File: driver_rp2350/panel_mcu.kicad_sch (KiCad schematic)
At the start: 33 parts, among them SW1 SW_Push, SW2 SW_Push, U1 APS6404L-3SQR, U2 RP2354B_80QFN, Y1 ABM8-272-T3

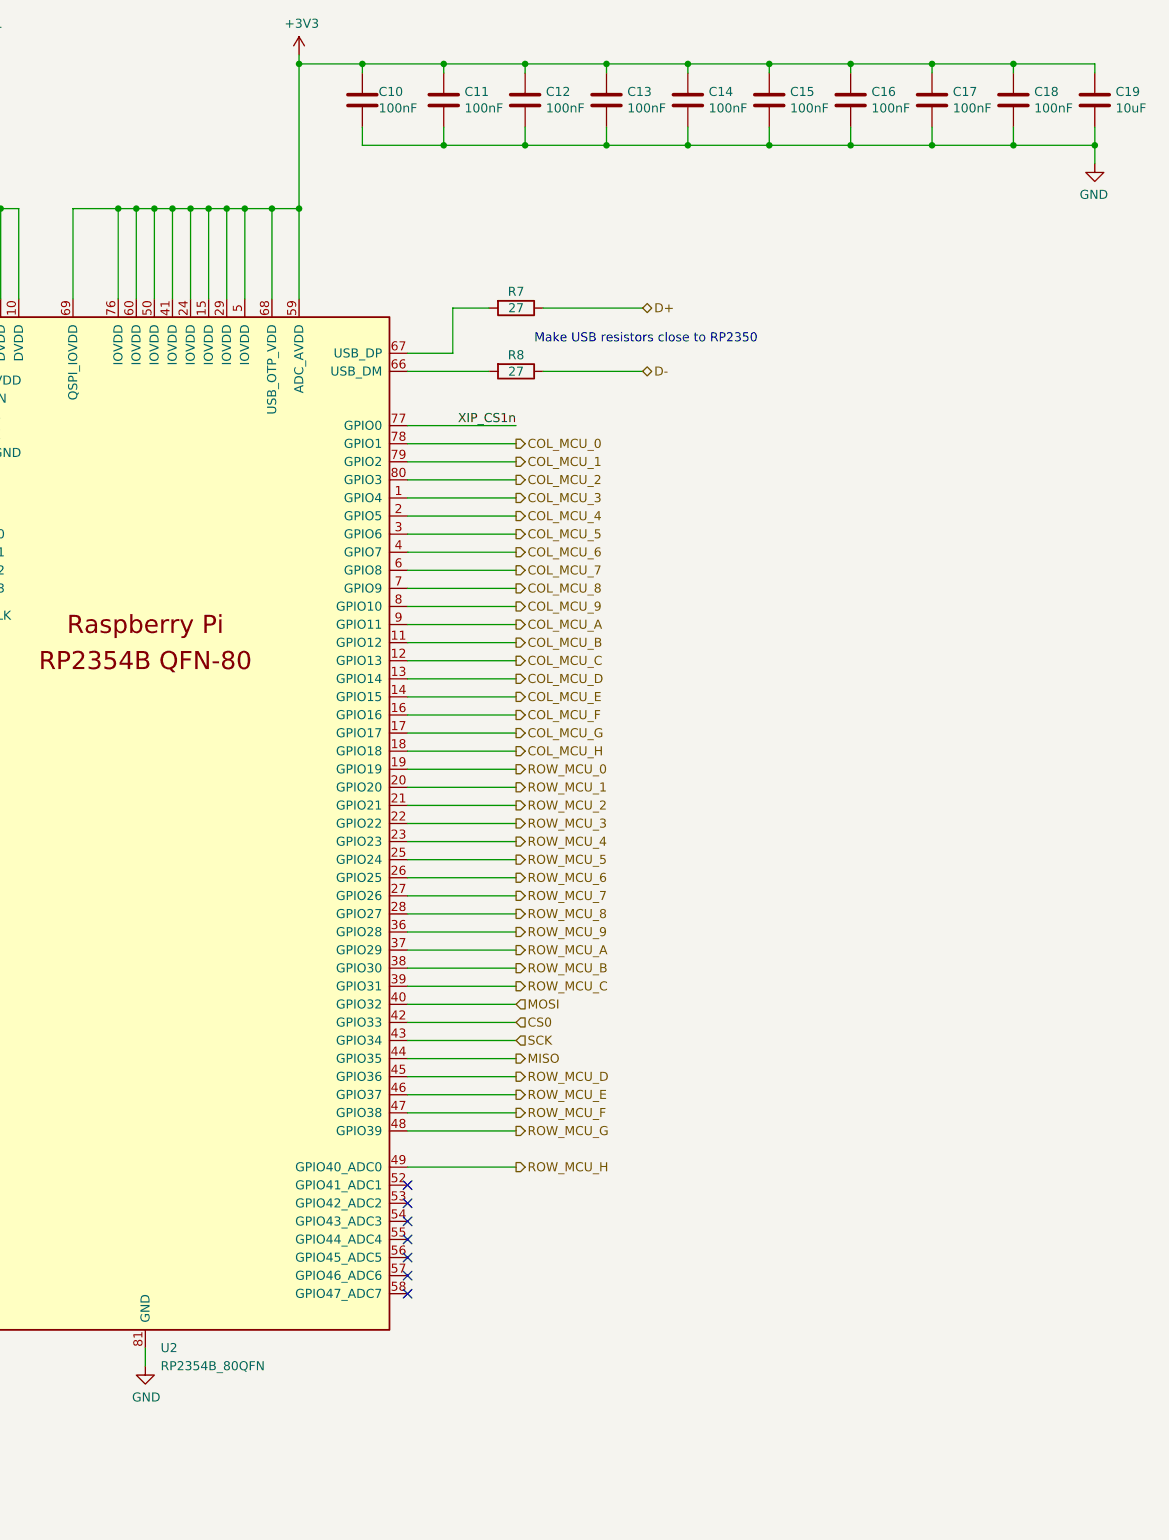
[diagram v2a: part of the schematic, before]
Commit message: Worked on layout for 18x18 rp2354b panels.
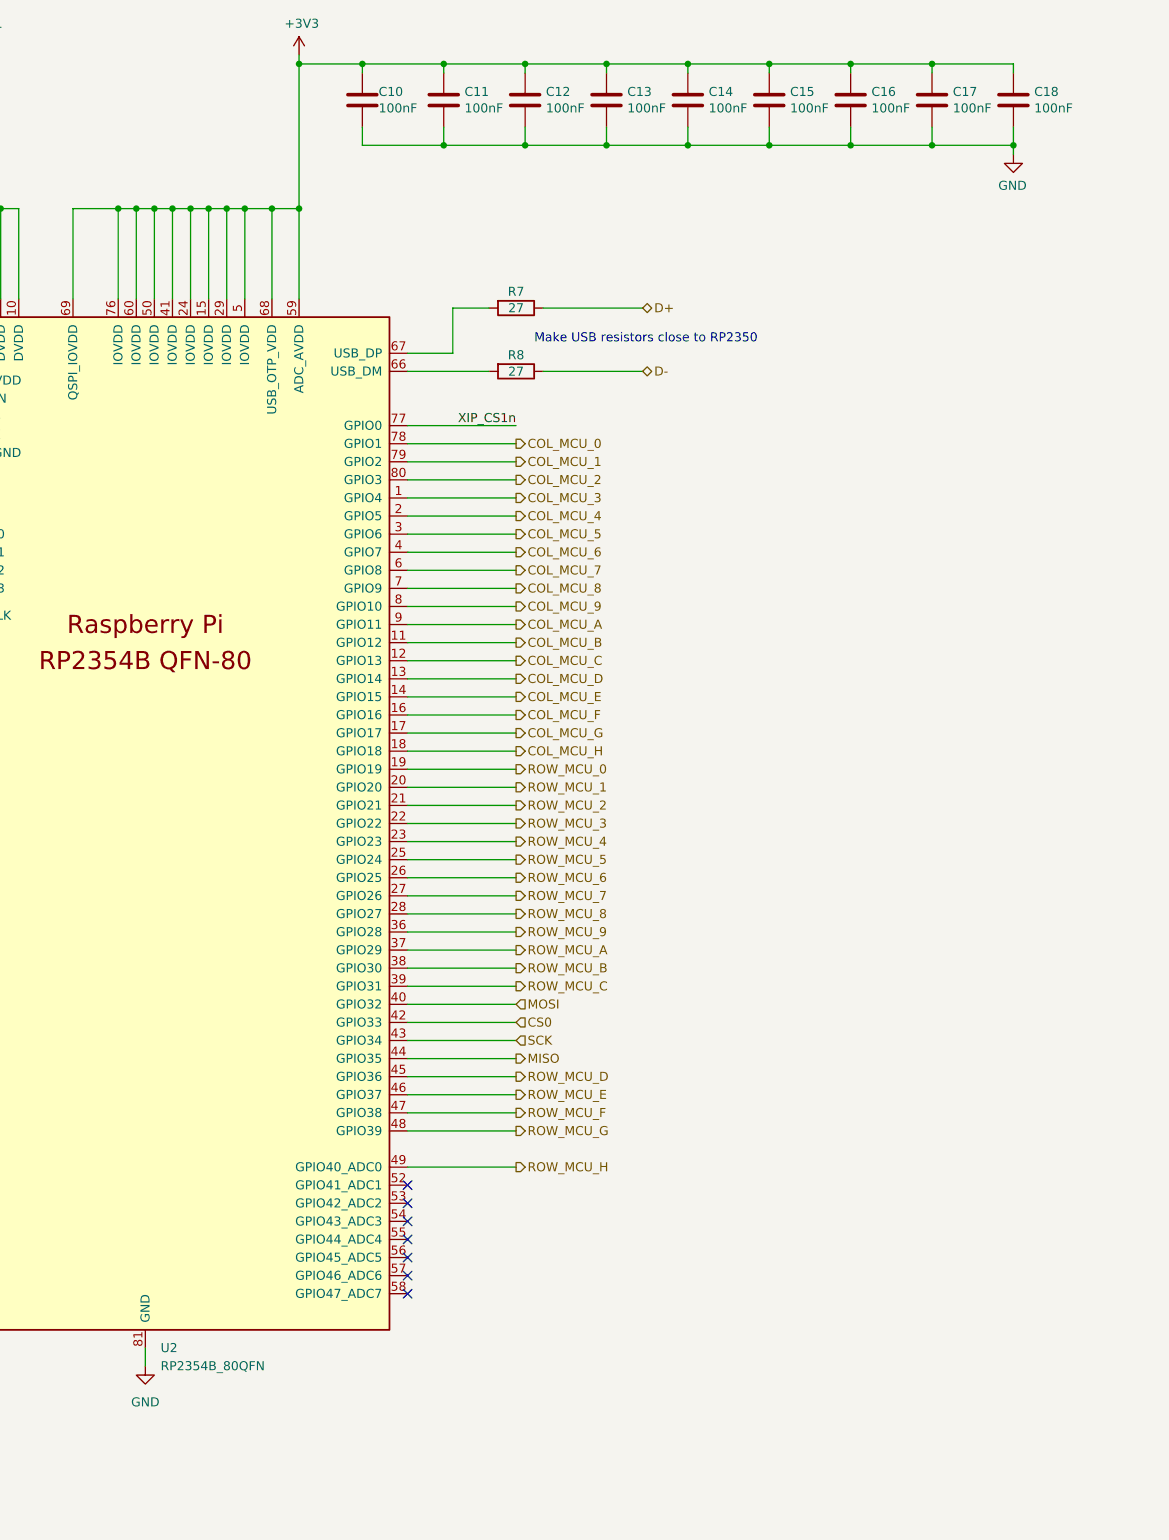
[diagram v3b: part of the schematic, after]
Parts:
- removed C19: 10uF, Capacitor_SMD:C_0402_1005Metric, symbol Device:C
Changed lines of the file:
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@@
 	)
 	(junction
-		(at 326.39 31.75)
-		(diameter 0)
-		(color 0 0 0 0)
-	)
-	(junction
 		(at 222.25 52.07)
 		(diameter 0)
@@
 	)
 	(junction
+		(at 326.39 43.18)
+		(diameter 0)
+		(color 0 0 0 0)
+	)
+	(junction
 		(at 140.97 73.66)
 		(diameter 0)
@@
 	)
 	(junction
-		(at 337.82 43.18)
-		(diameter 0)
-		(color 0 0 0 0)
-	)
-	(junction
 		(at 292.1 43.18)
 		(diameter 0)
@@
 	)
 	(junction
-		(at 326.39 43.18)
-		(diameter 0)
-		(color 0 0 0 0)
-	)
-	(junction
 		(at 280.67 31.75)
 		(diameter 0)
@@
 	(wire
 		(pts
+			(xy 326.39 43.18) (xy 326.39 44.45)
+		)
+		(stroke
+			(width 0)
+			(type default)
+		)
+	)
+	(wire
+		(pts
 			(xy 241.3 92.71) (xy 256.54 92.71)
 		)
@@
 	(wire
 		(pts
-			(xy 326.39 31.75) (xy 337.82 31.75)
-		)
-		(stroke
-			(width 0)
-			(type default)
-		)
-	)
-	(wire
-		(pts
 			(xy 241.3 135.89) (xy 256.54 135.89)
 		)
@@
 	(wire
 		(pts
-			(xy 337.82 43.18) (xy 337.82 45.72)
-		)
-		(stroke
-			(width 0)
-			(type default)
-		)
-	)
-	(wire
-		(pts
 			(xy 181.61 52.07) (xy 181.61 64.77)
 		)
@@
 	(wire
 		(pts
-			(xy 337.82 40.64) (xy 337.82 43.18)
-		)
-		(stroke
-			(width 0)
-			(type default)
-		)
-	)
-	(wire
-		(pts
 			(xy 158.75 100.33) (xy 172.72 100.33)
 		)
@@
 	(wire
 		(pts
-			(xy 337.82 31.75) (xy 337.82 33.02)
-		)
-		(stroke
-			(width 0)
-			(type default)
-		)
-	)
-	(wire
-		(pts
 			(xy 204.47 212.09) (xy 204.47 214.63)
 		)
@@
 	(wire
 		(pts
-			(xy 337.82 43.18) (xy 326.39 43.18)
-		)
-		(stroke
-			(width 0)
-			(type default)
-		)
-	)
-	(wire
-		(pts
 			(xy 68.58 170.18) (xy 82.55 170.18)
 		)
@@
 	)
 	(symbol
-		(lib_id "power:GND")
-		(at 204.47 214.63 0)
-		(unit 1)
-		(exclude_from_sim no)
-		(in_bom yes)
-		(on_board yes)
-		(dnp no)
-		(property "Reference" "#PWR018"
-			(at 204.47 220.98 0)
-			(effects
-				(font
-					(size 1.27 1.27)
-				)
-				(hide yes)
-			)
-		)
-		(property "Value" "GND"
-			(at 204.597 219.0242 0)
-			(effects
-				(font
-					(size 1.27 1.27)
-				)
-			)
-		)
-		(property "Footprint" ""
-			(at 204.47 214.63 0)
-			(effects
-				(font
-					(size 1.27 1.27)
-				)
-				(hide yes)
-			)
-		)
-		(property "Datasheet" ""
-			(at 204.47 214.63 0)
-			(effects
-				(font
-					(size 1.27 1.27)
-				)
-				(hide yes)
-			)
-		)
-		(property "Description" ""
-			(at 204.47 214.63 0)
-			(effects
-				(font
-					(size 1.27 1.27)
-				)
-			)
-		)
-		(pin "1"
-		)
-		(instances
-			(project "driver_rp2350"
-				(path "/1e634561-32a0-4ffa-9d4f-e93f355464d5/b30b56c6-21ca-46ed-bb1a-e5062fd43ea8"
-					(reference "#PWR018")
-					(unit 1)
-				)
-			)
-		)
-	)
-	(symbol
 		(lib_id "power:+3V3")
 		(at 226.06 30.48 0)
@@
 	)
 	(symbol
-		(lib_id "Device:C")
-		(at 337.82 36.83 0)
-		(unit 1)
-		(exclude_from_sim no)
-		(in_bom yes)
-		(on_board yes)
-		(dnp no)
-		(property "Reference" "C19"
-			(at 340.741 35.6616 0)
-			(effects
-				(font
-					(size 1.27 1.27)
-				)
-				(justify left)
-			)
-		)
-		(property "Value" "10uF"
-			(at 340.741 37.973 0)
-			(effects
-				(font
-					(size 1.27 1.27)
-				)
-				(justify left)
-			)
-		)
-		(property "Footprint" "Capacitor_SMD:C_0402_1005Metric"
-			(at 338.7852 40.64 0)
-			(effects
-				(font
-					(size 1.27 1.27)
-				)
-				(hide yes)
-			)
-		)
-		(property "Datasheet" "~"
-			(at 337.82 36.83 0)
-			(effects
-				(font
-					(size 1.27 1.27)
-				)
-				(hide yes)
-			)
-		)
-		(property "Description" ""
-			(at 337.82 36.83 0)
-			(effects
-				(font
-					(size 1.27 1.27)
-				)
-			)
-		)
-		(pin "1"
-		)
-		(pin "2"
-		)
-		(instances
-			(project "driver_rp2350"
-				(path "/1e634561-32a0-4ffa-9d4f-e93f355464d5/b30b56c6-21ca-46ed-bb1a-e5062fd43ea8"
-					(reference "C19")
-					(unit 1)
-				)
-			)
-		)
-	)
-	(symbol
 		(lib_id "power:+3V3")
 		(at 68.58 151.13 0)
@@
 	)
 	(symbol
+		(lib_name "GND_1")
+		(lib_id "power:GND")
+		(at 204.47 214.63 0)
+		(unit 1)
+		(exclude_from_sim no)
+		(in_bom yes)
+		(on_board yes)
+		(dnp no)
+		(fields_autoplaced yes)
+		(property "Reference" "#PWR03"
+			(at 204.47 220.98 0)
+			(effects
+				(font
+					(size 1.27 1.27)
+				)
+				(hide yes)
+			)
+		)
+		(property "Value" "GND"
+			(at 204.47 219.71 0)
+			(effects
+				(font
+					(size 1.27 1.27)
+				)
+			)
+		)
+		(property "Footprint" ""
+			(at 204.47 214.63 0)
+			(effects
+				(font
+					(size 1.27 1.27)
+				)
+				(hide yes)
+			)
+		)
+		(property "Datasheet" ""
+			(at 204.47 214.63 0)
+			(effects
+				(font
+					(size 1.27 1.27)
+				)
+				(hide yes)
+			)
+		)
+		(property "Description" "Power symbol creates a global label with name \"GND\" , ground"
+			(at 204.47 214.63 0)
+			(effects
+				(font
+					(size 1.27 1.27)
+				)
+				(hide yes)
+			)
+		)
+		(pin "1"
+		)
+		(instances
+			(project ""
+				(path "/1e634561-32a0-4ffa-9d4f-e93f355464d5/b30b56c6-21ca-46ed-bb1a-e5062fd43ea8"
+					(reference "#PWR03")
+					(unit 1)
+				)
+			)
+		)
+	)
+	(symbol
 		(lib_id "Device:R")
 		(at 256.54 66.04 270)
@@
 	(symbol
 		(lib_id "power:GND")
-		(at 337.82 45.72 0)
+		(at 326.39 44.45 0)
 		(mirror y)
 		(unit 1)
@@
 		(dnp no)
 		(property "Reference" "#PWR020"
-			(at 337.82 52.07 0)
+			(at 326.39 50.8 0)
 			(effects
 				(font
@@
 		)
 		(property "Value" "GND"
-			(at 337.693 50.1142 0)
+			(at 326.263 48.8442 0)
 			(effects
 				(font
@@
 		)
 		(property "Footprint" ""
-			(at 337.82 45.72 0)
+			(at 326.39 44.45 0)
 			(effects
 				(font
@@
 		)
 		(property "Datasheet" ""
-			(at 337.82 45.72 0)
+			(at 326.39 44.45 0)
 			(effects
 				(font
@@
 		)
 		(property "Description" ""
-			(at 337.82 45.72 0)
+			(at 326.39 44.45 0)
 			(effects
 				(font
